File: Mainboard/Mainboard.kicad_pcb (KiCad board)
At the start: 2 copper layers, 95 x 60 mm, 33 parts, among them IC1 MC7805BD2TR4G, IC2 MC7805BD2TR4G, J1 26-60-4023, J2 BHR-14-VUA, J3 26-60-4023, J4 4328, U1 ISO1541

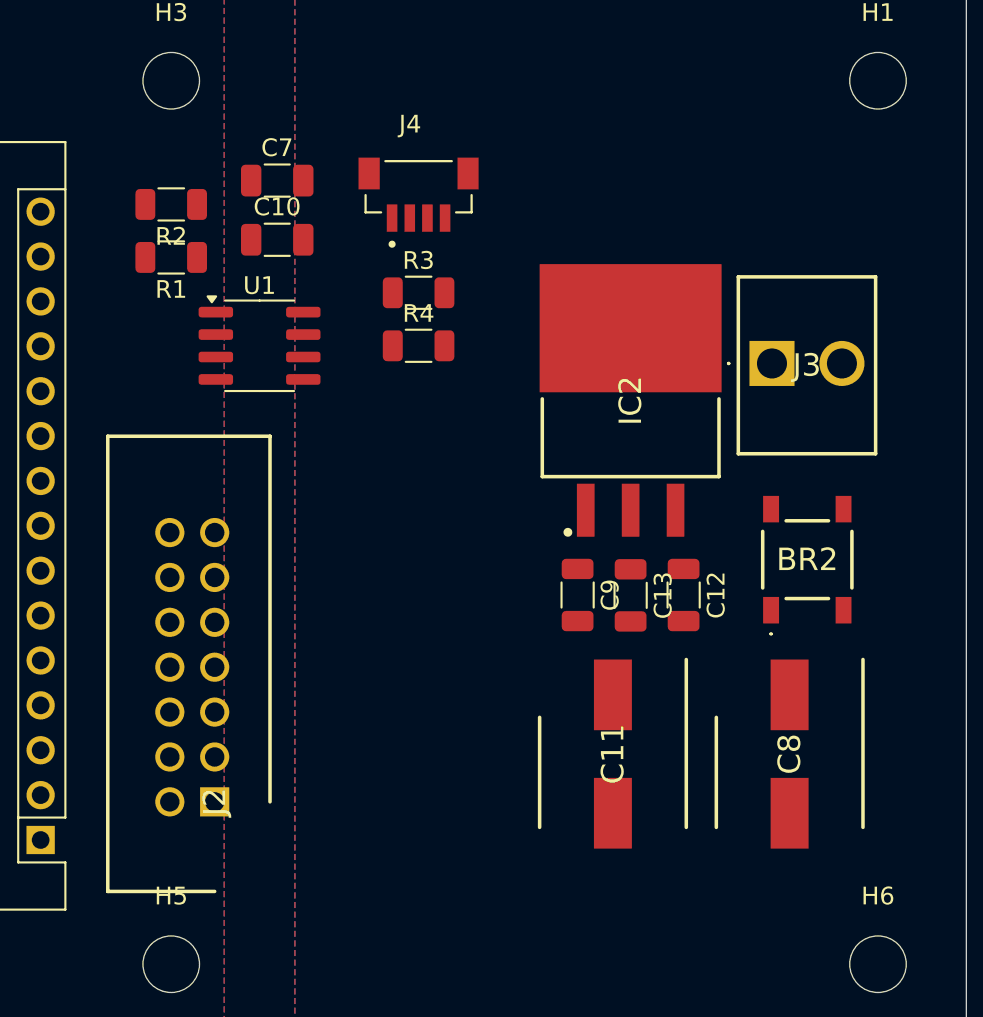
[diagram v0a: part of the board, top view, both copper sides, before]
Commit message: moving everything onto front panel, switching psu, no iso
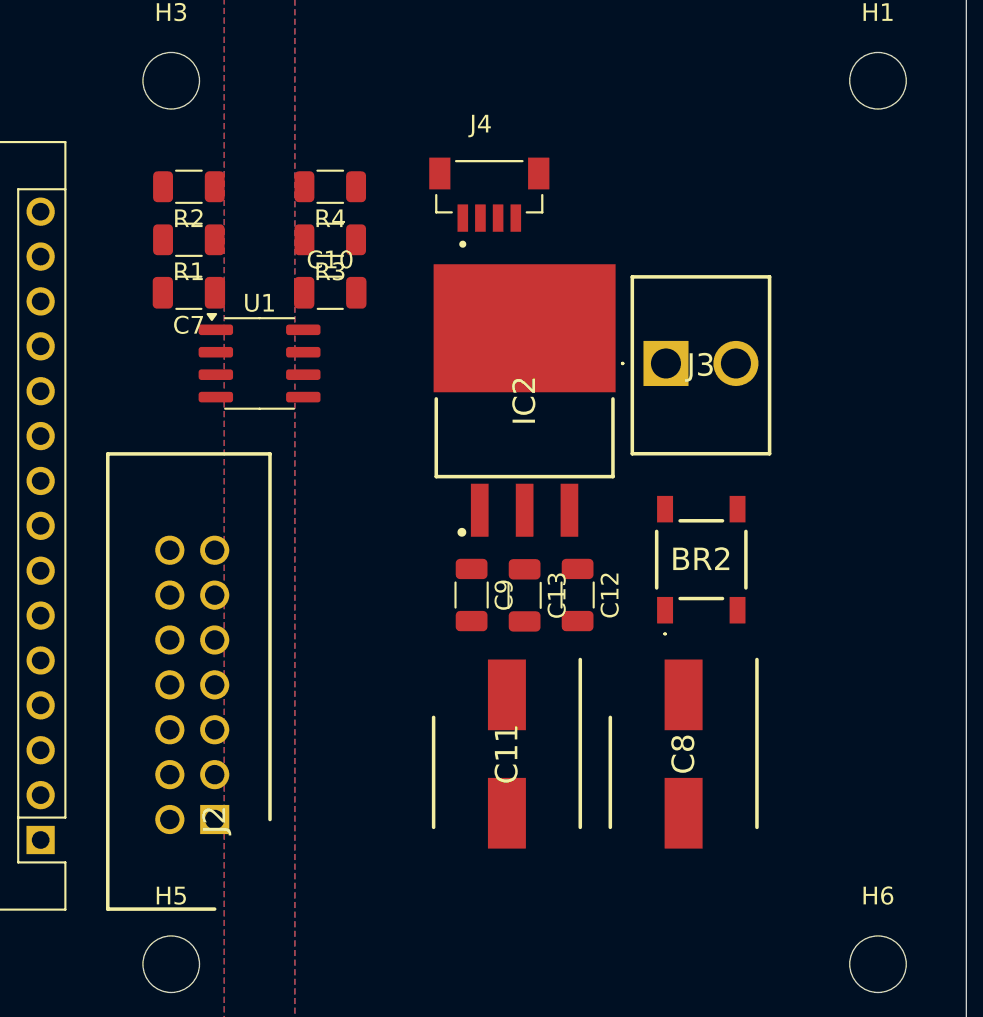
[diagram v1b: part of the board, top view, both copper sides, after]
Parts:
- moved R4 10.3 mm to (149.0, 66.0), turned to 180 degrees
- moved C7 8.08 mm to (141.0, 72.0), turned to 180 degrees
- moved BR2 6.00 mm to (170.0, 87.1)
- moved C11 6.00 mm to (159.0, 98.1)
- moved C12 6.00 mm to (163.0, 89.1)
- moved C13 6.00 mm to (160.0, 89.1)
- moved C8 6.00 mm to (169.0, 98.1)
- moved C9 6.00 mm to (157.0, 89.1)
- moved IC2 6.00 mm to (160.0, 78.1)
- moved J3 6.00 mm to (168.0, 76.0)
- moved R3 5.83 mm to (149.0, 69.0), turned to 180 degrees
- moved C10 4.24 mm to (149.0, 72.0)
- moved J4 4.00 mm to (158.0, 66.0)
- moved R1 1.41 mm to (141.0, 69.0)
- moved R2 1.41 mm to (141.0, 66.0)
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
